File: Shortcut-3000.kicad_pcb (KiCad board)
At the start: 2 copper layers, 33 parts, among them SW1 SW_Push, SW10 SW_Push, SW11 SW_Push, SW12 SW_Push, SW13 SW_Push, SW14 SW_Push, SW15 SW_Push, SW16 RotaryEncoder_Switch, SW17 RotaryEncoder_Switch, SW2 SW_Push, SW3 SW_Push, SW4 SW_Push, SW5 SW_Push, SW6 SW_Push, SW7 SW_Push, SW8 SW_Push, SW9 SW_Push

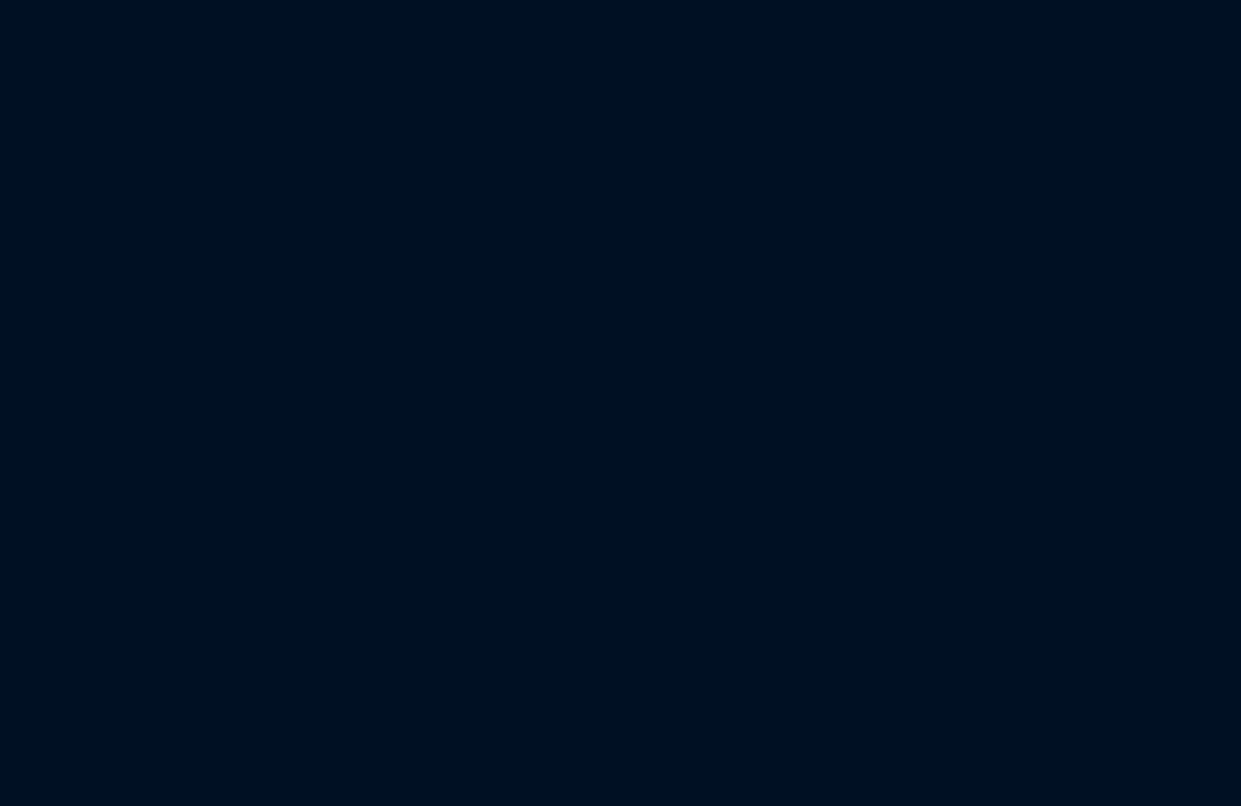
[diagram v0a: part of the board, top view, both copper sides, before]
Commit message: Lay out magnetic connectors as a 4x3 module grid
Schematic: J1-J12 rearranged into 4 columns x 3 rows (J1-J4 top row).
PCB: J1-J12 placed on a 25.4mm-pitch grid, each connector centred
along the top edge of its cell with N (pin 1) on the left. Cell
outlines drawn on Cmts.User. Pico GP14/GP15/3V3 pads now carry the
SDA/SCL/+3V3 nets.
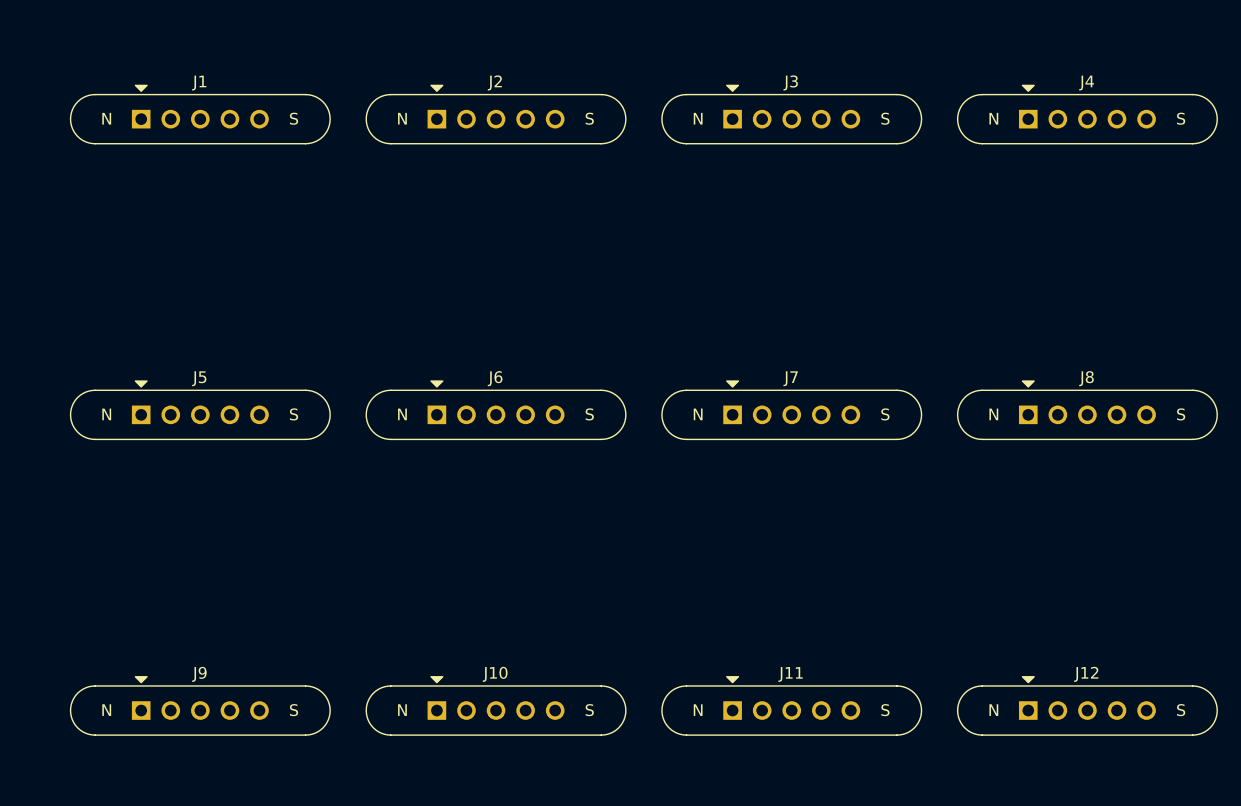
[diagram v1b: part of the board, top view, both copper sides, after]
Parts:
- added J1: MagneticPogo_1x05_Female, Shortcut-3000:MagneticPogo_1x05_P2.54mm_Female, F.Cu at (282.7, 22.0)
- added J10: MagneticPogo_1x05_Female, Shortcut-3000:MagneticPogo_1x05_P2.54mm_Female, F.Cu at (308.1, 72.8)
- added J11: MagneticPogo_1x05_Female, Shortcut-3000:MagneticPogo_1x05_P2.54mm_Female, F.Cu at (333.5, 72.8)
- added J12: MagneticPogo_1x05_Female, Shortcut-3000:MagneticPogo_1x05_P2.54mm_Female, F.Cu at (358.9, 72.8)
- added J2: MagneticPogo_1x05_Female, Shortcut-3000:MagneticPogo_1x05_P2.54mm_Female, F.Cu at (308.1, 22.0)
- added J3: MagneticPogo_1x05_Female, Shortcut-3000:MagneticPogo_1x05_P2.54mm_Female, F.Cu at (333.5, 22.0)
- added J4: MagneticPogo_1x05_Female, Shortcut-3000:MagneticPogo_1x05_P2.54mm_Female, F.Cu at (358.9, 22.0)
- added J5: MagneticPogo_1x05_Female, Shortcut-3000:MagneticPogo_1x05_P2.54mm_Female, F.Cu at (282.7, 47.4)
- added J6: MagneticPogo_1x05_Female, Shortcut-3000:MagneticPogo_1x05_P2.54mm_Female, F.Cu at (308.1, 47.4)
- added J7: MagneticPogo_1x05_Female, Shortcut-3000:MagneticPogo_1x05_P2.54mm_Female, F.Cu at (333.5, 47.4)
- added J8: MagneticPogo_1x05_Female, Shortcut-3000:MagneticPogo_1x05_P2.54mm_Female, F.Cu at (358.9, 47.4)
- added J9: MagneticPogo_1x05_Female, Shortcut-3000:MagneticPogo_1x05_P2.54mm_Female, F.Cu at (282.7, 72.8)
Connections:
- A1 pad 19: unconnected-(A1-GPIO14-Pad19) -> /SDA
- A1 pad 20: unconnected-(A1-GPIO15-Pad20) -> /SCL
- A1 pad 36: unconnected-(A1-3V3-Pad36) -> +3V3
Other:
- board text added: "Module grid 4 x 3, 25.4 mm pitch"
